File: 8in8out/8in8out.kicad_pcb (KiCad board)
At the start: 2 copper layers, 62 parts, among them IC1 ATTINY48-A, J1 RJ45, J2 RJ45, J3 CONN_6, K110 G5T-1-12VDC, K120 G5T-1-12VDC, K130 G5T-1-12VDC, K140 G5T-1-12VDC, K150 G5T-1-12VDC, K160 G5T-1-12VDC, K170 G5T-1-12VDC, K180 G5T-1-12VDC, P1 CONN_5, P100 CONN_2, P101 CONN_2, P102 CONN_2, P103 CONN_2, P105 CONN_2, P106 CONN_2, P110 CONN_2, P120 CONN_2, P130 CONN_2, P140 CONN_2, P150 CONN_2, P160 CONN_2, P170 CONN_2, P180 CONN_2, P2 CONN_5, P3 CONN_10X2, P4 CONN_2, U1 7805, U10 OPTO-TRANSISTOR, U2 ULN2803, U20 OPTO-TRANSISTOR, U30 OPTO-TRANSISTOR, U40 OPTO-TRANSISTOR, U50 OPTO-TRANSISTOR, U60 OPTO-TRANSISTOR, U70 OPTO-TRANSISTOR, U80 OPTO-TRANSISTOR

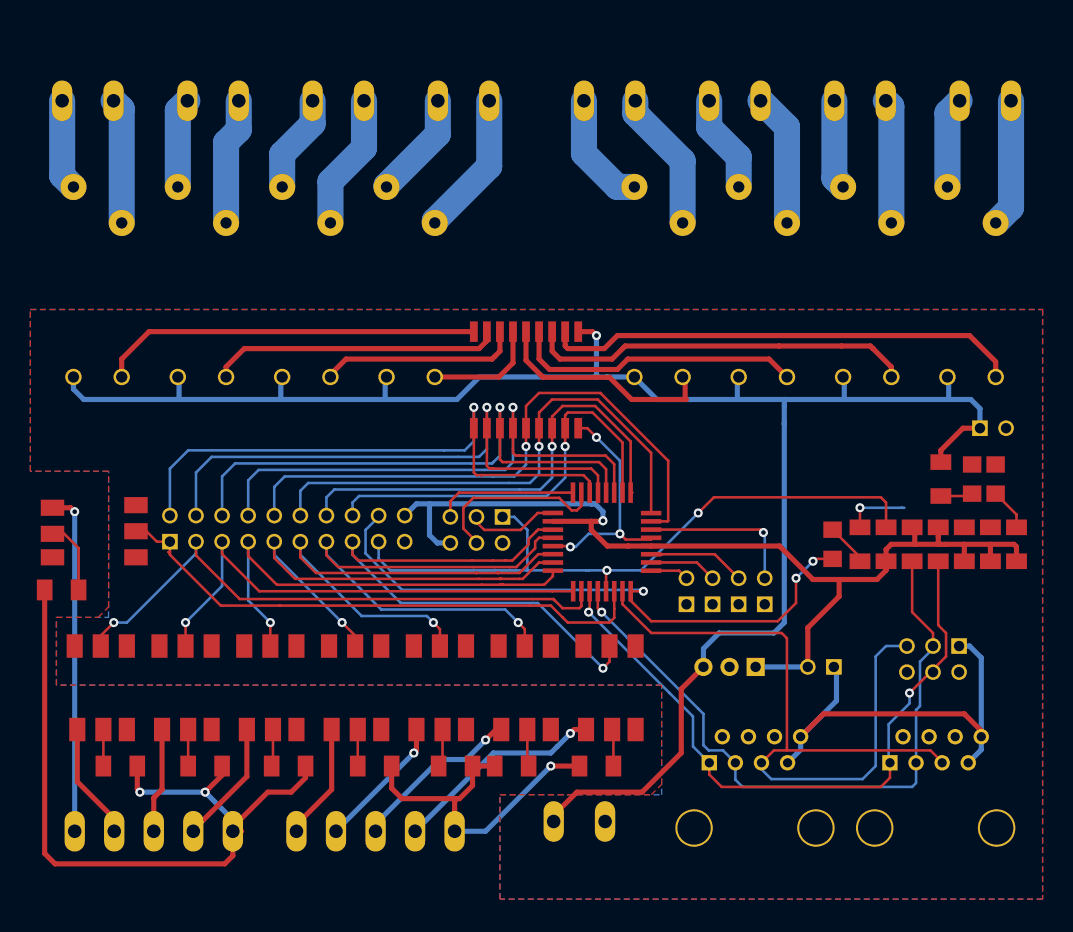
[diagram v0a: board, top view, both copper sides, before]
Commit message: Changement connecteur 12v par modele 3.85mm
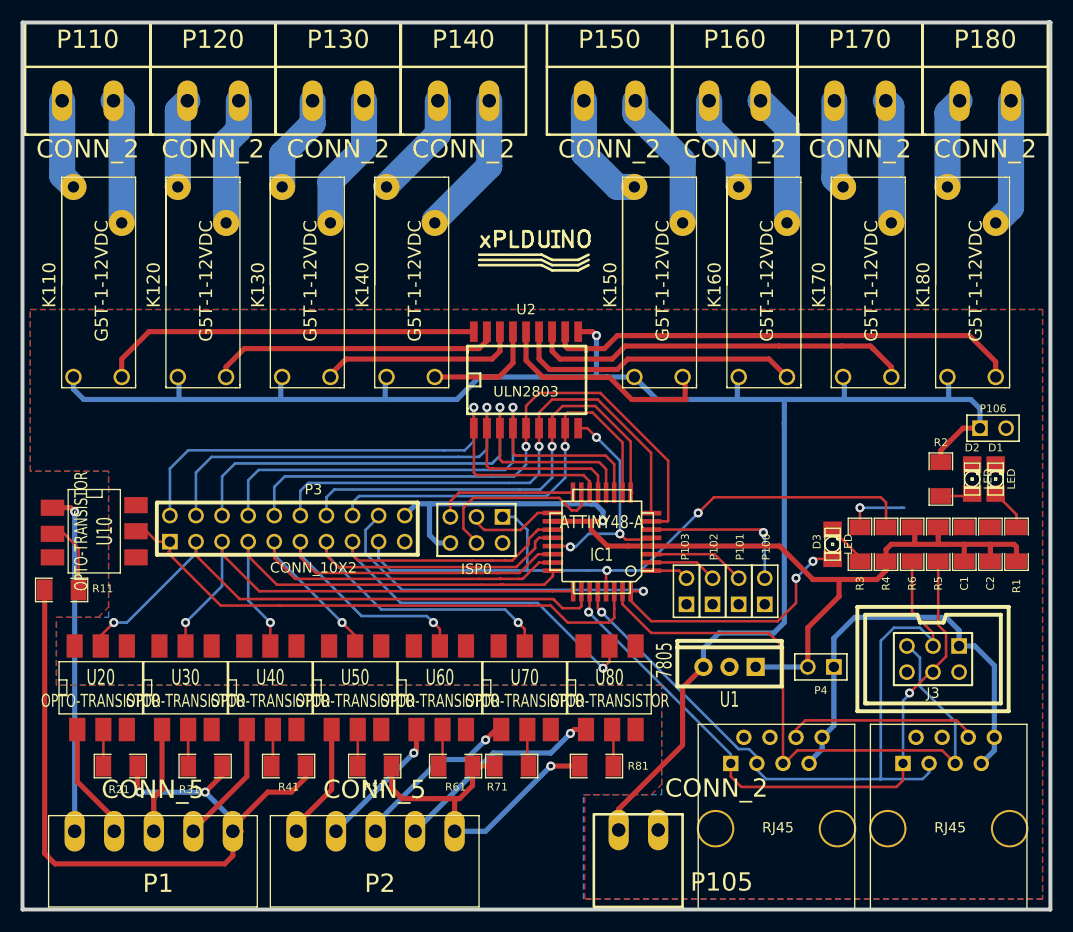
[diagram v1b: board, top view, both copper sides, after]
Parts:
- P105: footprint MOL_CONN_2_VH -> MOL_CONN_2_MINI
- moved P105 5.77 mm to (241.6, 149.7)
- moved J2 2.10 mm to (255.0, 149.6)
- moved J1 1.27 mm to (271.8, 149.6)
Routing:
- net GND: track 29.2 -> 48.1 mm
- net /INT: track 75.0 -> 61.2 mm
- net SCL: track 65.9 -> 72.1 mm
- net +12V: track 177.5 -> 172.0 mm
- net 5V_EXT: track 44.6 -> 42.5 mm
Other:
- board outline added: 100.1 x 86.4 mm
